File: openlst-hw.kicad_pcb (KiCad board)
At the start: 4 copper layers, 80 x 80 mm, 156 parts, among them J1 Conn_02x24_Odd_Even, J10 EXT 5V, J11 EXT VRF, J12 EXT VBAT, J13 MS UART1, J16 MS Prog/Debug, J2 EXT 3V3, J3 UART0, J4 MS UART0, J5 Switch Select, J6 Control Outputs, J7 CC Prog/Debug, J8 Conn_Coaxial, J9 ANT, U1 AP63205WU, U10 AP63200WU, U11 MSPM0G3107SDGS20R, U12 TJA1051TK-3, U2 CC1110, U3 0433BM15A0001, U4 MIC803, U5 PE4250MLI, U6 PE4250MLI, U7 SF2446E, U8 RFFM6406, U9 AP63203WU, X1 TG2520SMN 27MHz

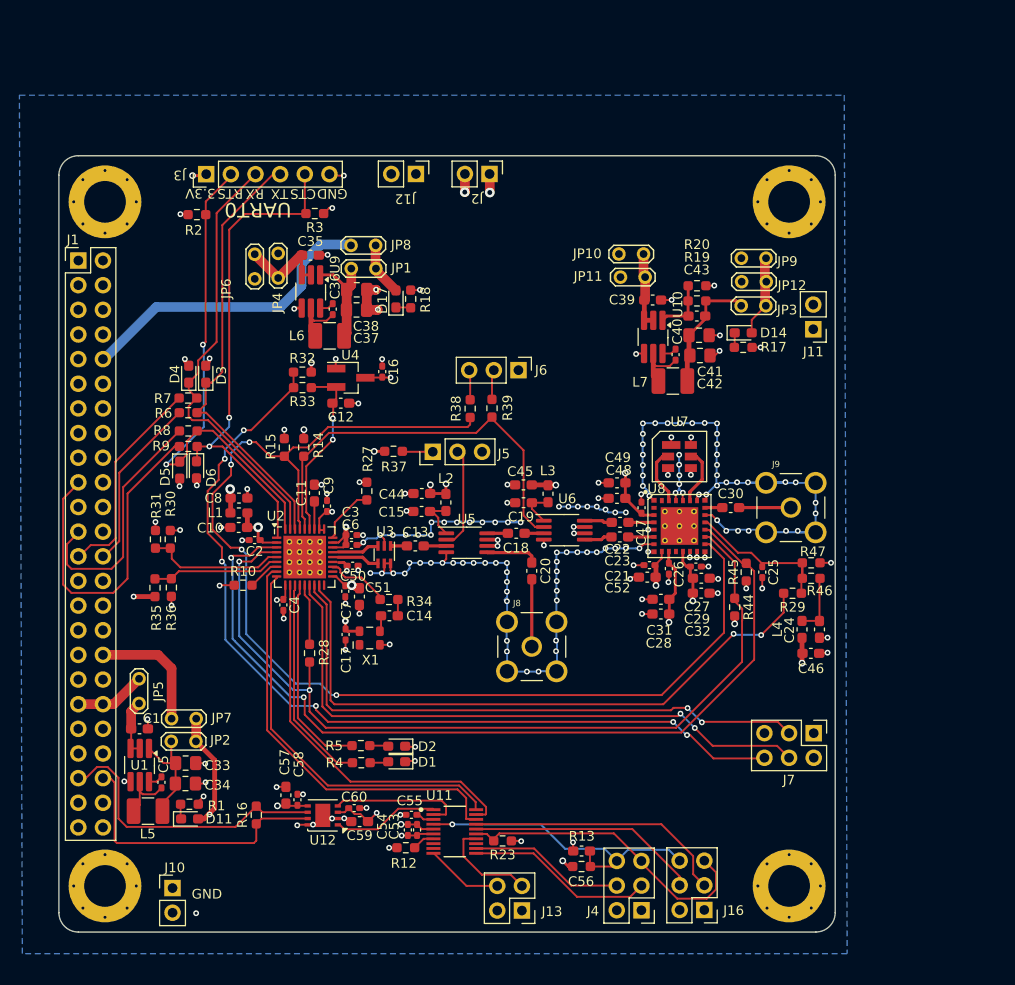
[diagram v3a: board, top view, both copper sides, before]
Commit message: cleanup, logical arrangement of connectors, short paths where possible and step files for all components
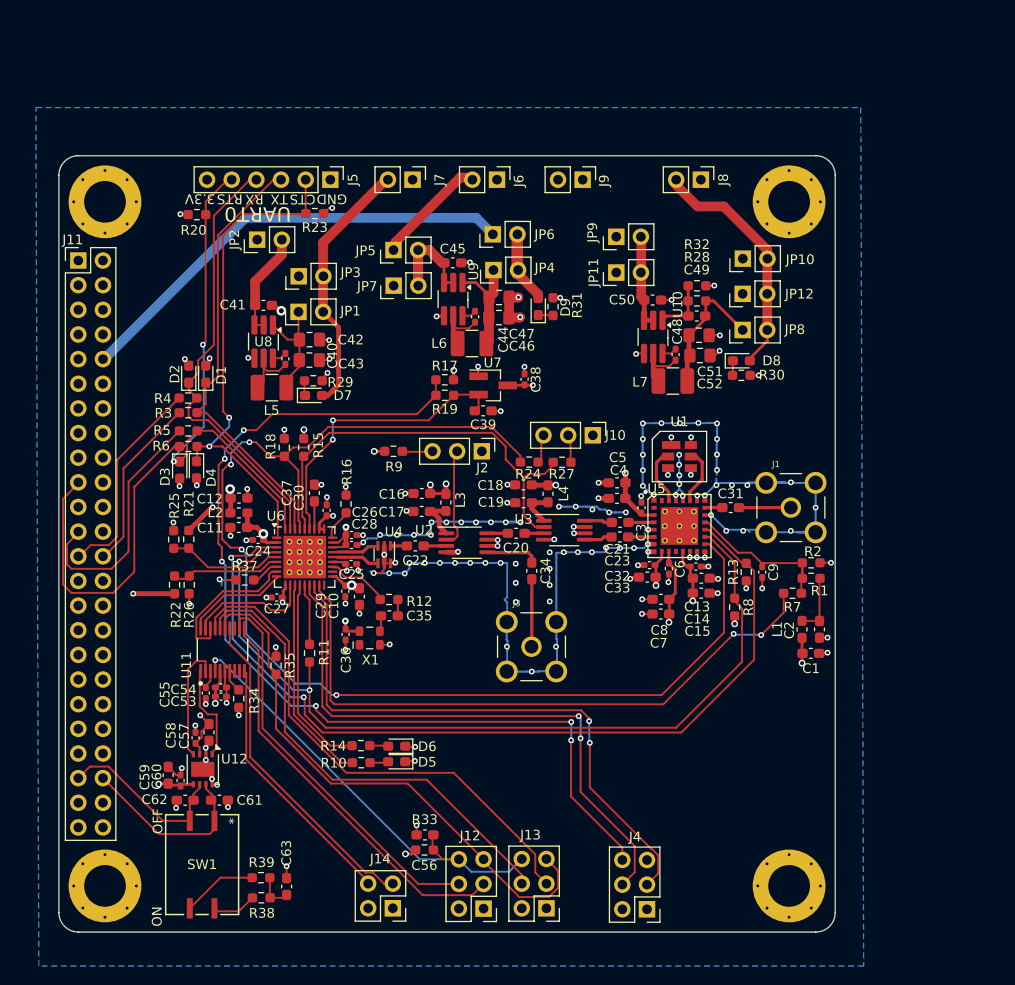
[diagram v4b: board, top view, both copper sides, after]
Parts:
- removed the C58 at (84.6, 126.4)
- removed the J10 at (71.7, 135.5)
- removed the J11 at (137.7, 77.9)
- removed the J12 at (96.8, 61.9)
- removed the J2 at (104.4, 61.9)
- removed the J3 at (75.2, 61.9)
- removed the R16 at (80.3, 127.9)
- added C60: 100n, Capacitor_SMD:C_0402_1005Metric_Pad0.74x0.62mm_HandSolder, F.Cu at (72.5, 124.4)
- added C61: 100p, Capacitor_SMD:C_0603_1608Metric_Pad1.08x0.95mm_HandSolder, F.Cu at (76.5, 126.4)
- added C62: 100p, Capacitor_SMD:C_0603_1608Metric_Pad1.08x0.95mm_HandSolder, F.Cu at (73.0, 126.4)
- added C63: 4n7, Capacitor_SMD:C_0603_1608Metric_Pad1.08x0.95mm_HandSolder, F.Cu at (83.5, 135.3)
- added J5: UART0, Connector_PinHeader_2.54mm:PinHeader_1x06_P2.54mm_Vertical, F.Cu at (88.0, 62.5)
- added J6: EXT VBAT, Connector_PinHeader_2.54mm:PinHeader_1x02_P2.54mm_Vertical, F.Cu at (105.2, 62.5)
- added J7: EXT 5V, Connector_PinHeader_2.54mm:PinHeader_1x02_P2.54mm_Vertical, F.Cu at (96.4, 62.5)
- added J8: EXT VRF, Connector_PinHeader_2.54mm:PinHeader_1x02_P2.54mm_Vertical, F.Cu at (126.2, 62.5)
- added J9: EXT 3V3, Connector_PinHeader_2.54mm:PinHeader_1x02_P2.54mm_Vertical, F.Cu at (114.0, 62.5)
- added R38: 60R4, Resistor_SMD:R_0603_1608Metric_Pad0.98x0.95mm_HandSolder, F.Cu at (80.9, 136.5)
- added R39: 60R4, Resistor_SMD:R_0603_1608Metric_Pad0.98x0.95mm_HandSolder, F.Cu at (80.8, 134.4)
- added SW1: 204-211ST, Project:SW4_204-211ST_CTS, F.Cu at (74.8, 133.1)
- JP1: renamed from JP2; footprint TestPoint:TestPoint_2Pads_Pitch2.54mm_Drill0.8mm -> Connector_PinHeader_2.54mm:PinHeader_1x02_P2.54mm_Vertical
- JP10: renamed from JP9; footprint TestPoint:TestPoint_2Pads_Pitch2.54mm_Drill0.8mm -> Connector_PinHeader_2.54mm:PinHeader_1x02_P2.54mm_Vertical
- JP11, JP12: footprint TestPoint:TestPoint_2Pads_Pitch2.54mm_Drill0.8mm -> Connector_PinHeader_2.54mm:PinHeader_1x02_P2.54mm_Vertical
- JP2: renamed from JP5; footprint TestPoint:TestPoint_2Pads_Pitch2.54mm_Drill0.8mm -> Connector_PinHeader_2.54mm:PinHeader_1x02_P2.54mm_Vertical
- JP3: renamed from JP7; footprint TestPoint:TestPoint_2Pads_Pitch2.54mm_Drill0.8mm -> Connector_PinHeader_2.54mm:PinHeader_1x02_P2.54mm_Vertical
- JP4: renamed from JP1; footprint TestPoint:TestPoint_2Pads_Pitch2.54mm_Drill0.8mm -> Connector_PinHeader_2.54mm:PinHeader_1x02_P2.54mm_Vertical
- JP5: renamed from JP4; footprint TestPoint:TestPoint_2Pads_Pitch2.54mm_Drill0.8mm -> Connector_PinHeader_2.54mm:PinHeader_1x02_P2.54mm_Vertical
- JP6: renamed from JP8; footprint TestPoint:TestPoint_2Pads_Pitch2.54mm_Drill0.8mm -> Connector_PinHeader_2.54mm:PinHeader_1x02_P2.54mm_Vertical
- JP7: renamed from JP6; footprint TestPoint:TestPoint_2Pads_Pitch2.54mm_Drill0.8mm -> Connector_PinHeader_2.54mm:PinHeader_1x02_P2.54mm_Vertical
- JP8: renamed from JP3; footprint TestPoint:TestPoint_2Pads_Pitch2.54mm_Drill0.8mm -> Connector_PinHeader_2.54mm:PinHeader_1x02_P2.54mm_Vertical
- JP9: renamed from JP10; footprint TestPoint:TestPoint_2Pads_Pitch2.54mm_Drill0.8mm -> Connector_PinHeader_2.54mm:PinHeader_1x02_P2.54mm_Vertical
- moved JP3 47.4 mm to (84.7, 72.4), turned to 90 degrees
- moved JP2 46.9 mm to (80.4, 68.7), turned to 90 degrees
- moved JP1 46.2 mm to (84.7, 76.1), turned to 90 degrees
- moved C40 45.5 mm to (83.3, 80.9)
- moved C41 45.5 mm to (81.1, 75.4)
- moved C42 45.5 mm to (85.8, 79.0)
- moved C43 45.5 mm to (85.8, 81.1)
- moved D7 45.5 mm to (86.2, 84.7)
- moved L5 45.5 mm to (82.0, 83.9)
- moved R29 45.5 mm to (86.2, 83.2)
- moved U8 45.5 mm to (81.1, 79.2)
- moved U11 30.4 mm to (76.9, 110.9), turned to 90 degrees
- moved R35 29.5 mm to (82.4, 112.5), turned to -90 degrees
- moved J4 25.0 mm to (120.6, 137.7), turned to 180 degrees
- moved C54 25.0 mm to (76.7, 114.8), turned to 0 degrees
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- renumbered C46 to C1, C51 to C10, C10 to C11, C8 to C12, C27 to C13, C29 to C14, C32 to C15, C44 to C16, C15 to C17, C45 to C18, C24 to C2, C18 to C20, C22 to C21, C13 to C22, C2 to C24, C50 to C25, C3 to C26, C4 to C27, C6 to C28, C7 to C29, C47 to C3, C9 to C30, C30 to C31, C21 to C32, C52 to C33, C20 to C34, C14 to C35, C17 to C36, C11 to C37, C16 to C38, C12 to C39, C48 to C4, C5 to C40, C1 to C41, C33 to C42, C34 to C43, C36 to C44, C35 to C45, C37 to C46, C38 to C47, C40 to C48, C43 to C49, C49 to C5, C39 to C50, C41 to C51, C42 to C52, C54 to C53, C53 to C54, C59 to C57, C60 to C58, C57 to C59, C26 to C6, C28 to C7, C31 to C8, C25 to C9, D3 to D1, D4 to D2, D5 to D3, D6 to D4, D1 to D5, D2 to D6, D11 to D7, D14 to D8, D17 to D9, J9 to J1, J6 to J10, J1 to J11, J4 to J12, J16 to J13, J13 to J14, J5 to J2, J8 to J3, J7 to J4, L4 to L1, L1 to L2, L2 to L3, L3 to L4, R46 to R1, R4 to R10, R28 to R11, R34 to R12, R45 to R13, R5 to R14, R14 to R15, R27 to R16, R32 to R17, R15 to R18, R33 to R19, R47 to R2, R2 to R20, R30 to R21, R35 to R22, R3 to R23, R38 to R24, R31 to R25, R36 to R26, R39 to R27, R19 to R28, R1 to R29, R6 to R3, R17 to R30, R18 to R31, R20 to R32, R13 to R33, R12 to R34, R23 to R35, R10 to R37, R7 to R4, R8 to R5, R9 to R6, R29 to R7, R44 to R8, R37 to R9, U7 to U1, U5 to U2, U6 to U3, U3 to U4, U8 to U5, U2 to U6, U4 to U7, U1 to U8
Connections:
- net VRF renamed +VRF
- J11 pad 37: VBAT -> GND
- J11 pad 38: VBAT -> /INTERBOARD_CONNECTOR2/5V0_2
- J11 pad 4: unconnected-(J1-Pin_4-Pad4) -> BATT
- J11 pad 45: unconnected-(J1-Pin_45-Pad45) -> /INTERBOARD_CONNECTOR2/CAN2L
- J11 pad 46: unconnected-(J1-Pin_46-Pad46) -> /INTERBOARD_CONNECTOR2/CAN2H
- J2 pad 1: Net-(J5-Pin_1) -> GND
- J2 pad 3: GND -> Net-(J2-Pin_3)
- JP2 pad 1: VBAT -> BATT
- R9 pad 2: Net-(J5-Pin_1) -> Net-(J2-Pin_3)
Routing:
- net 5V0: track 12.7 -> 53.1 mm
- net UART1_TX: track 40.9 -> 10.7 mm
- net UART1_RTS: track 43.7 -> 15.3 mm
- net UART1_RX: track 39.7 -> 12.9 mm
- net /UART-CAN/SWDIO: track 24.0 -> 49.9 mm
- net /UART-CAN/SWCLK: track 27.3 -> 53.1 mm
- net /UART-CAN/BSL: track 32.1 -> 56.8 mm
- net /UART-CAN/MS_UART0_RX: track 16.1 -> 40.7 mm
- net /UART-CAN/MS_UART1_TX: track 10.3 -> 34.2 mm
- net /UART-CAN/MS_UART0_TX: track 19.4 -> 41.9 mm
- net +5V: track 154.4 -> 132.7 mm, vias 2 -> 1
- net /UART-CAN/MS_UART1_RX: track 7.92 -> 27.2 mm
- net BATT: track 0.00 -> 17.8 mm
- net 3V3: track 31.7 -> 46.8 mm
- net /UART-CAN/RST_N: track 32.3 -> 46.9 mm
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
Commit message: break out RF part to separate schema, update BOM
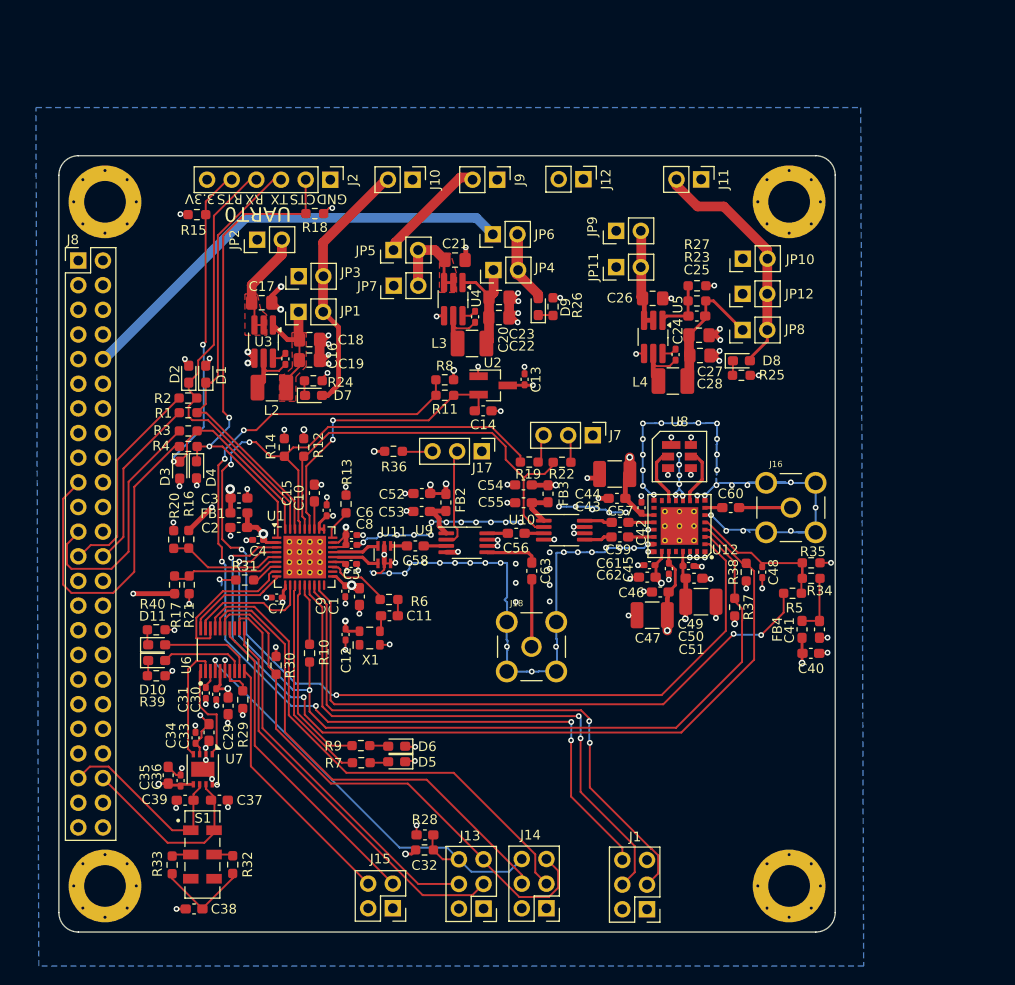
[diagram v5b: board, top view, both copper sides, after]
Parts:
- removed the C41 at (81.1, 75.4)
- removed the C45 at (100.6, 71.0)
- removed the C50 at (121.2, 74.9)
- removed J6: EXT VBAT, Connector_PinHeader_2.54mm:PinHeader_1x02_P2.54mm_Vertical
- removed the J7 at (96.4, 62.5)
- removed the J8 at (126.2, 62.5)
- removed SW1: 204-211ST, Project:SW4_204-211ST_CTS
- added C17: 10u, Capacitor_SMD:C_0805_2012Metric_Pad1.18x1.45mm_HandSolder, F.Cu at (80.9, 75.2)
- added C21: 10u, Capacitor_SMD:C_0805_2012Metric_Pad1.18x1.45mm_HandSolder, F.Cu at (100.8, 70.8)
- added C26: 10u, Capacitor_SMD:C_0805_2012Metric_Pad1.18x1.45mm_HandSolder, F.Cu at (121.2, 74.7)
- added D10: ORANGE, LED_SMD:LED_0603_1608Metric_Pad1.05x0.95mm_HandSolder, F.Cu at (70.1, 112.0)
- added D11: ORANGE, LED_SMD:LED_0603_1608Metric_Pad1.05x0.95mm_HandSolder, F.Cu at (70.1, 110.4)
- added J10: EXT 5V, Connector_PinHeader_2.54mm:PinHeader_1x02_P2.54mm_Vertical, F.Cu at (96.4, 62.5)
- added J11: EXT VRF, Connector_PinHeader_2.54mm:PinHeader_1x02_P2.54mm_Vertical, F.Cu at (126.2, 62.4)
- added J12: EXT 3V3, Connector_PinHeader_2.54mm:PinHeader_1x02_P2.54mm_Vertical, F.Cu at (114.0, 62.4)
- added R39: 680, Resistor_SMD:R_0603_1608Metric_Pad0.98x0.95mm_HandSolder, F.Cu at (70.0, 113.6)
- added R40: 680, Resistor_SMD:R_0603_1608Metric_Pad0.98x0.95mm_HandSolder, F.Cu at (70.0, 108.8)
- added S1: JS202011JCQN, Project:SW_JS202011JCQN, F.Cu at (74.8, 132.0)
- C29: renamed from C53; footprint Capacitor_SMD:C_0402_1005Metric_Pad0.74x0.62mm_HandSolder -> Capacitor_SMD:C_0603_1608Metric_Pad1.08x0.95mm_HandSolder
- C44: renamed from C5; footprint Capacitor_SMD:C_0603_1608Metric_Pad1.08x0.95mm_HandSolder -> Capacitor_SMD:C_1210_3225Metric_Pad1.33x2.70mm_HandSolder
- C47: renamed from C8; footprint Capacitor_SMD:C_0603_1608Metric_Pad1.08x0.95mm_HandSolder -> Capacitor_SMD:C_1210_3225Metric_Pad1.33x2.70mm_HandSolder
- C51: renamed from C15; footprint Capacitor_SMD:C_0603_1608Metric_Pad1.08x0.95mm_HandSolder -> Capacitor_SMD:C_1210_3225Metric_Pad1.33x2.70mm_HandSolder
- D7, D8: value GREEN V4 -> GREEN
- D9: value GREEN V3 -> GREEN
- J9: value EXT 3V3 -> EXT VBAT
- R10: renamed from R11; value DNP -> 0
- R24: renamed from R29; value 1k5 -> 1K5
- R28: renamed from R33; value 47k -> 47K
- R29: renamed from R34; value 100k -> 100K
- R30: renamed from R35; value 47k -> 47K
- R5: renamed from R7; value DNP -> 0
- moved C38 9.82 mm to (73.9, 137.6), turned to 180 degrees
- moved R33 9.25 mm to (71.7, 133.1), turned to 90 degrees
- moved J9 8.80 mm to (105.2, 62.5)
- moved R32 4.51 mm to (77.9, 133.1), turned to 90 degrees
- moved C46 2.27 mm to (122.0, 105.0)
- moved C47 1.87 mm to (121.1, 107.3)
- moved C29 1.20 mm to (77.4, 116.7), turned to -90 degrees
- moved C44 0.94 mm to (117.3, 92.8)
- moved C51 0.88 mm to (126.2, 106.0)
- moved C30 0.86 mm to (76.2, 115.5), turned to -90 degrees
- moved C49 0.76 mm to (124.9, 102.3)
- moved C50 0.75 mm to (125.5, 103.5)
- moved JP9 0.61 mm to (117.4, 67.7)
- moved JP11 0.56 mm to (117.4, 71.5)
- moved R29 0.43 mm to (79.0, 116.1)
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- renumbered C10 to C1, C30 to C10, C35 to C11, C36 to C12, C38 to C13, C39 to C14, C37 to C15, C40 to C16, C42 to C18, C43 to C19, C11 to C2, C44 to C20, C46 to C22, C47 to C23, C48 to C24, C49 to C25, C51 to C27, C52 to C28, C12 to C3, C54 to C30, C55 to C31, C56 to C32, C57 to C33, C58 to C34, C59 to C35, C60 to C36, C61 to C37, C63 to C38, C62 to C39, C24 to C4, C1 to C40, C2 to C41, C3 to C42, C4 to C43, C6 to C45, C7 to C46, C9 to C48, C13 to C49, C25 to C5, C14 to C50, C16 to C52, C17 to C53, C18 to C54, C19 to C55, C20 to C56, C21 to C57, C22 to C58, C23 to C59, C26 to C6, C31 to C60, C32 to C61, C33 to C62, C34 to C63, C27 to C7, C28 to C8, C29 to C9, L2 to FB1, L3 to FB2, L4 to FB3, L1 to FB4, J4 to J1, J12 to J13, J13 to J14, J14 to J15, J1 to J16, J2 to J17, J3 to J18, J5 to J2, J10 to J7, J11 to J8, L5 to L2, L6 to L3, L7 to L4, R3 to R1, R19 to R11, R15 to R12, R16 to R13, R18 to R14, R20 to R15, R21 to R16, R22 to R17, R23 to R18, R24 to R19, R4 to R2, R25 to R20, R26 to R21, R27 to R22, R28 to R23, R30 to R25, R31 to R26, R32 to R27, R5 to R3, R37 to R31, R38 to R32, R39 to R33, R1 to R34, R2 to R35, R9 to R36, R8 to R37, R13 to R38, R6 to R4, R12 to R6, R10 to R7, R17 to R8, R14 to R9, U6 to U1, U3 to U10, U4 to U11, U5 to U12, U7 to U2, U8 to U3, U9 to U4, U10 to U5, U11 to U6, U12 to U7, U1 to U8, U2 to U9
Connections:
- net /LST_TX_MODE renamed LST_TX_MODE
- net /RF_BYP renamed RF_BYP
- net /RF_EN renamed RF_EN
- net /~{LST_RESET} renamed LST_RESET
- net /~{LST_RX_MODE} renamed LST_RX_MODE
- net Net-(U6-RF_N) renamed RF_N
- net Net-(U6-RF_P) renamed RF_P
- C48 pad 1: /PA_VAPC -> PA_VAPC
- J9 pad 2: +3V3 -> +VBAT
- R34 pad 2: /PA_VAPC -> PA_VAPC
- R35 pad 1: /PA_VAPC -> PA_VAPC
- R5 pad 1: /PA_VAPC -> Net-(U1-P2_3/XOSC32-1)
- R5 pad 2: Net-(U6-P2_3/XOSC32-1) -> PA_VAPC
- U1 pad 17: Net-(U6-P2_3/XOSC32-1) -> Net-(U1-P2_3/XOSC32-1)
- U12 pad 5: /PA_VAPC -> PA_VAPC
- U6 pad 8: unconnected-(U11-PA5_HFXIN_FCC_IN-Pad8) -> /UART-CAN/MS_LED1
- U6 pad 9: unconnected-(U11-PA6_HFCLK_IN_HFXOUT-Pad9) -> /UART-CAN/MS_LED2
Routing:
- net Net-(U6-P2_3/XOSC32-1): track 65.3 -> 0.00 mm, vias 2 -> 0
- net Net-(U1-P2_3/XOSC32-1): track 0.00 -> 65.3 mm, vias 0 -> 2
- net PA_VAPC: track 0.00 -> 16.2 mm
- net /PA_VAPC: track 16.2 -> 0.00 mm
- net GND: track 242.9 -> 257.1 mm, vias 169 -> 181
- net /UART-CAN/MS_LED2: track 0.00 -> 9.63 mm
- net /UART-CAN/MS_LED1: track 0.00 -> 8.76 mm
- net Net-(C38-Pad1): track 3.90 -> 9.87 mm
- net Net-(R33-Pad2): track 7.92 -> 1.99 mm
- net +VRF: track 105.4 -> 110.5 mm
- net Net-(R32-Pad2): track 4.79 -> 1.97 mm
- net CAN_H: track 18.3 -> 20.0 mm
- net Net-(D10-K): track 0.00 -> 1.60 mm
- net CAN_L: track 18.5 -> 20.1 mm
- net Net-(D11-K): track 0.00 -> 1.58 mm
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- added copper zone on F.Cu, net +VBAT
- added copper zone on F.Cu, net Net-(JP1-A)
- added copper zone on F.Cu, net Net-(JP5-B)

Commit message: further refactor schema into subsheets
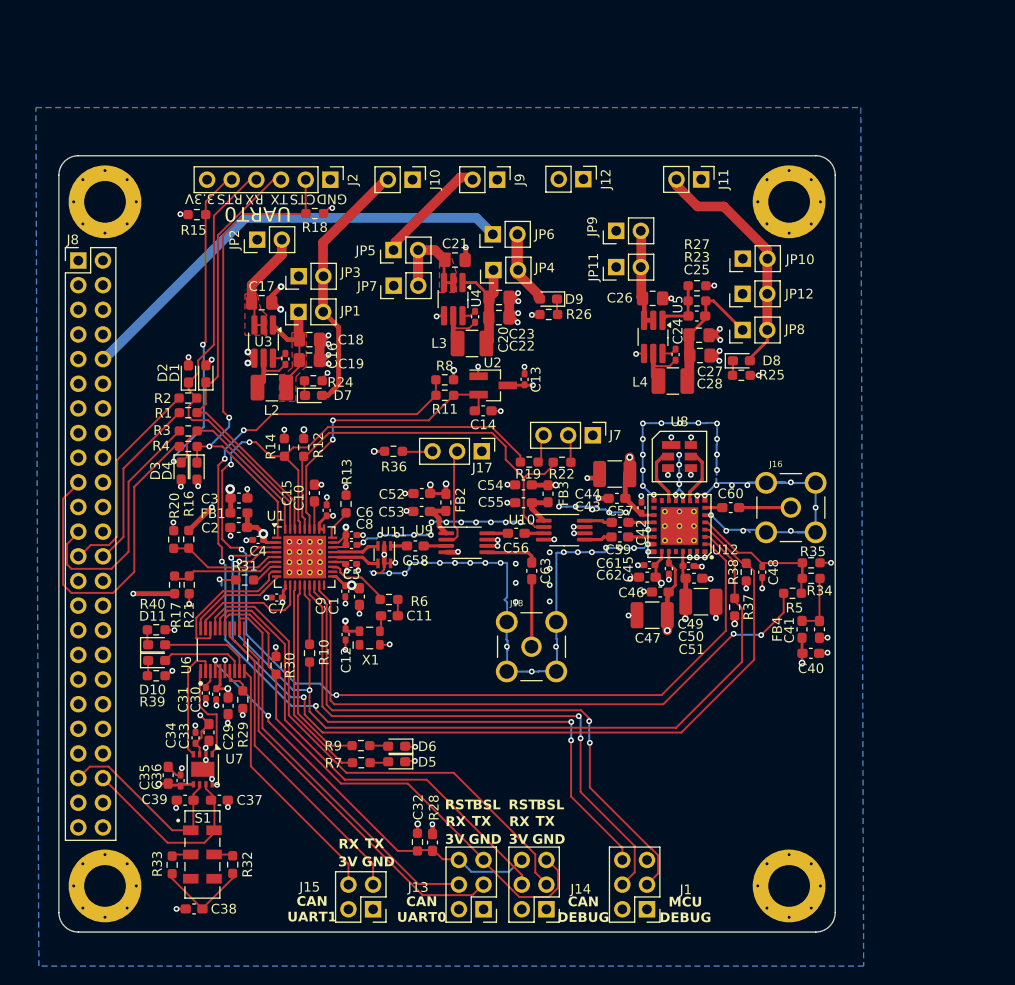
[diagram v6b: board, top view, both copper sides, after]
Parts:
- moved J15 2.03 mm to (92.4, 137.7)
- moved D9 1.31 mm to (110.5, 74.8), turned to 180 degrees
- moved C32 1.10 mm to (98.5, 130.8), turned to 90 degrees
- moved R28 1.09 mm to (97.0, 130.7), turned to -90 degrees
- moved R26 0.92 mm to (110.5, 76.4), turned to 180 degrees
- moved D3 0.17 mm to (72.6, 92.5)
- moved D4 0.14 mm to (74.2, 92.5)
- moved J14 0.10 mm to (110.2, 137.7)
- moved J13 0.07 mm to (103.8, 137.7)
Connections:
- net /+3V3_C1110 renamed /MCU/+3V3_C1110
- net /AN0 renamed AN0
- net /AN1 renamed AN1
- net /PROG_DC renamed PROG_DC
- net /PROG_DD renamed PROG_DD
- net /UART0_CTS renamed UART0_CTS
- net /UART0_RTS renamed UART0_RTS
- net /UART0_RX renamed UART0_RX
- net /UART0_TX renamed UART0_TX
- net Net-(U1-P0_6) renamed LED1
- net Net-(U1-P0_7) renamed LED2
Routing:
- net /UART-CAN/RST_N: track 47.1 -> 42.8 mm, vias 1 -> 2
- net /UART-CAN/MS_UART1_TX: track 33.3 -> 32.5 mm
- net /UART-CAN/MS_UART1_RX: track 27.2 -> 26.4 mm
- net /UART-CAN/SWDIO: track 49.9 -> 49.2 mm
- net /UART-CAN/BSL: track 56.8 -> 56.2 mm
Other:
- board text added: "3V"
- board text added: "BSL"
- board text added: "CAN DEBUG"
- board text added: "CAN UART0"
- board text added: "CAN UART1"
- board text added: "MCU DEBUG"
- board text added: "RST"
